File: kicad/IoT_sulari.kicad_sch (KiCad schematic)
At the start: 2 parts, among them U1 NRF9160-SICA-B1A-R, U2 TCR2EF33

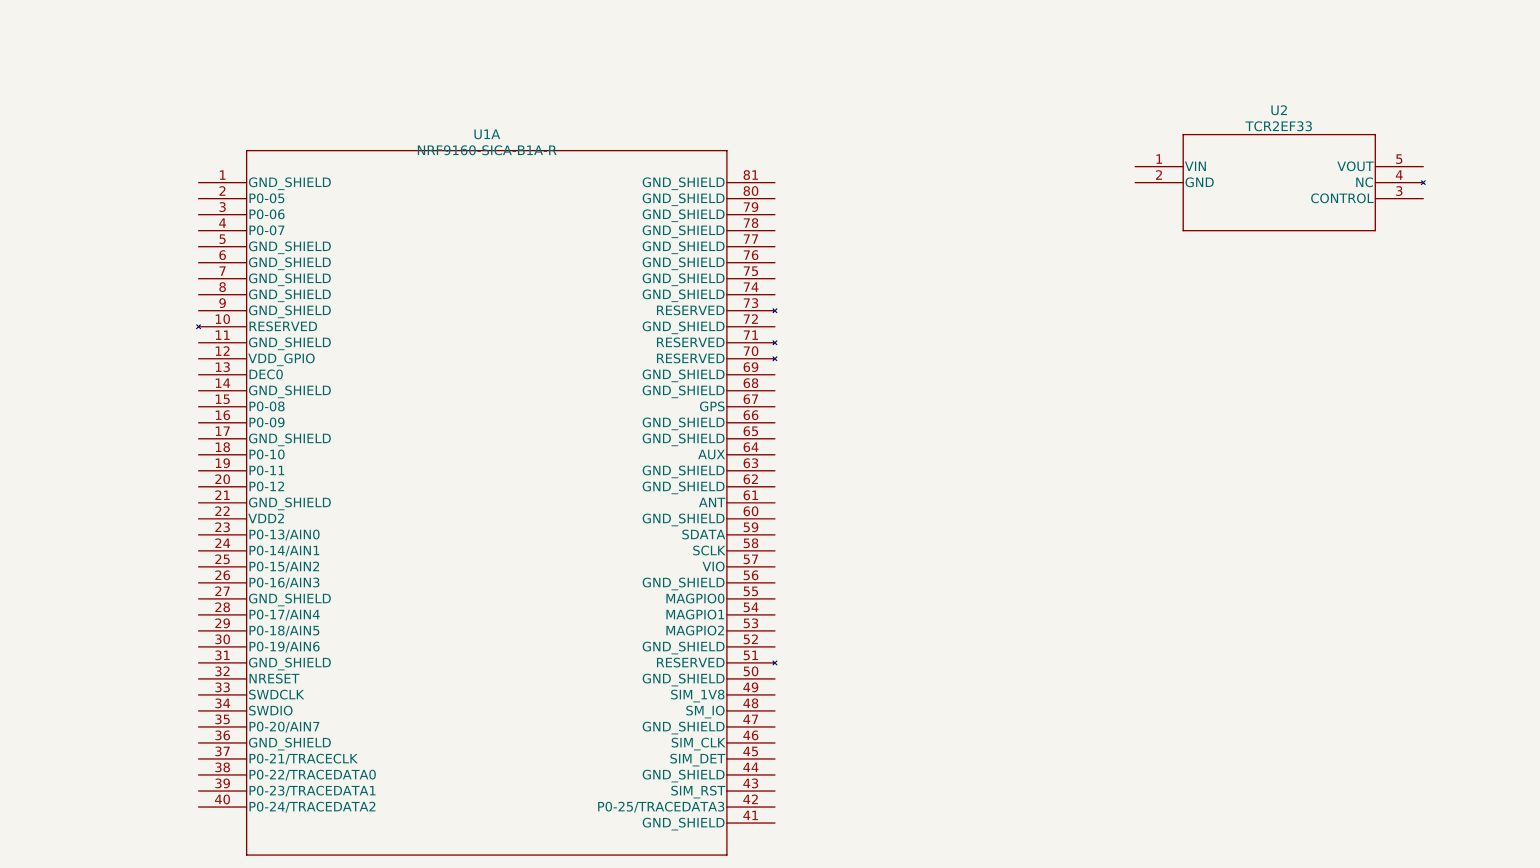
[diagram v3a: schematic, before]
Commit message: Added TMP117, HDC2010, TPD3F3 and TCR2EF33 symbols to KiCad and component documents to doc.
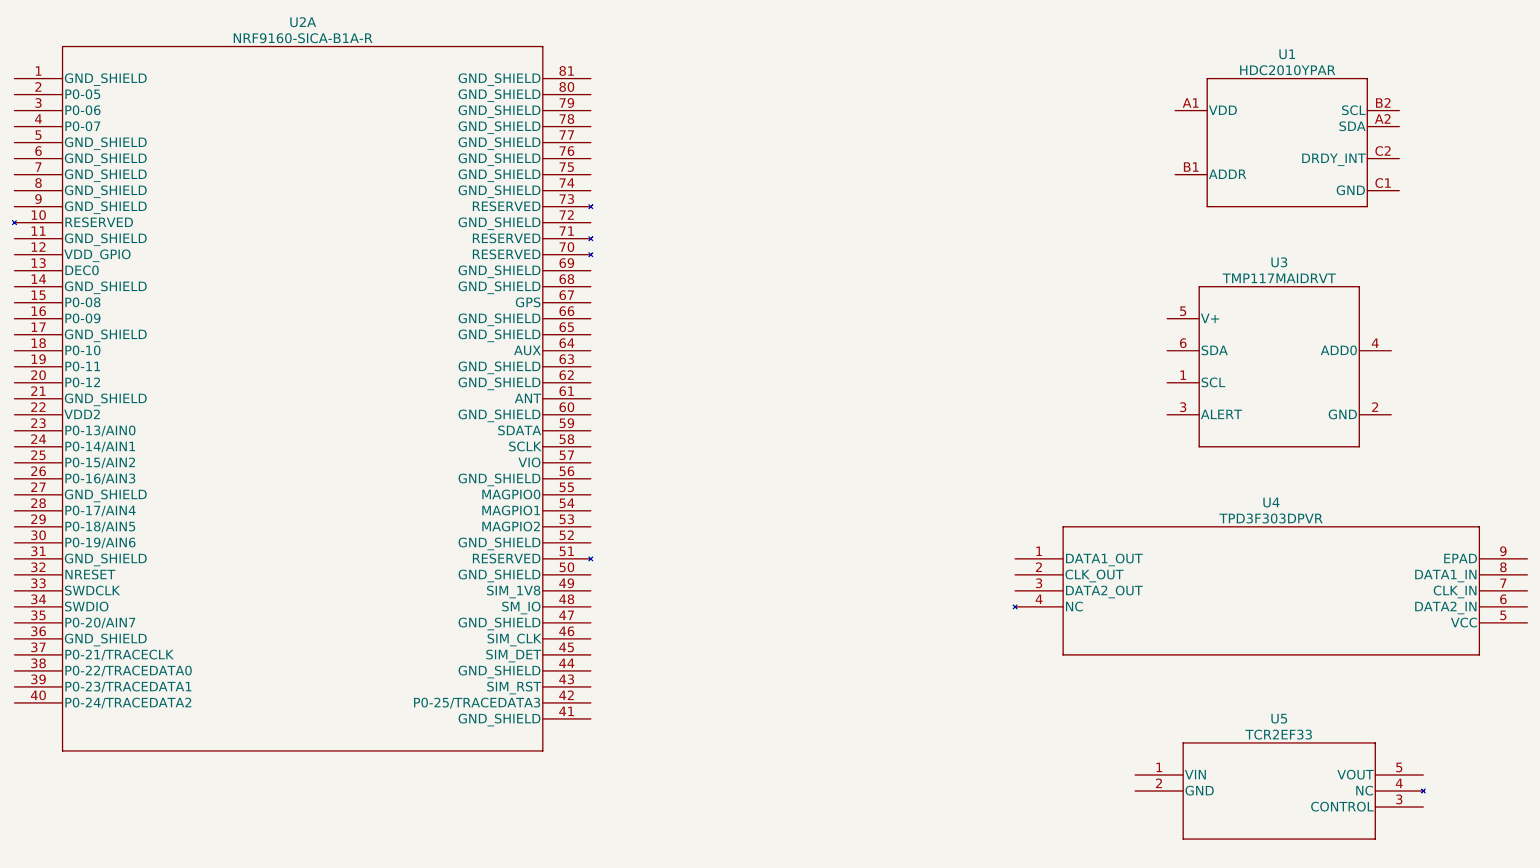
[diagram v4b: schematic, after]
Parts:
- removed U1: NRF9160-SICA-B1A-R, LGA_16X10P5_NOR, symbol NRF-9160-SICA-B1A-R:NRF9160-SICA-B1A-R
- removed U2: TCR2EF33, SOT-25 SMV_TOS, symbol TCR2EF33:TCR2EF33
- added U1: HDC2010YPAR, HDC2010YPAR:HDC2020YPAR, symbol HDC2010YPAR:HDC2010YPAR
- added U2: NRF9160-SICA-B1A-R, NRF-9160-SICA-B1A-R:NRF9160-SICA-B1A-R, symbol NRF-9160-SICA-B1A-R:NRF9160-SICA-B1A-R
- added U3: TMP117MAIDRVT, TMP117MAIDRVT:TMP117MAIDRVT, symbol TMP117MAIDRVT:TMP117MAIDRVT
- added U4: TPD3F303DPVR, TPD3F303DPVR:TPD3F303DPVR, symbol TPD3F303DPVR:TPD3F303DPVR
- added U5: TCR2EF33, TCR2EF33:TCR2EF33, symbol TCR2EF33:TCR2EF33
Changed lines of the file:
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@@
 (kicad_sch (version 20230121) (generator eeschema)
   (paper "A4")
-  (symbol (lib_id "TCR2EF33:TCR2EF33") (at 210.82 40.64 0) (unit 1)
-    (in_bom yes) (on_board yes) (dnp no) (fields_autoplaced)
-    (property "Reference" "U2" (at 233.68 31.75 0)
-      (effects (font (size 1.524 1.524)))
-    )
-    (property "Value" "TCR2EF33" (at 233.68 34.29 0)
-      (effects (font (size 1.524 1.524)))
-    )
-    (property "Footprint" "SOT-25   SMV_TOS" (at 233.68 34.544 0)
-      (effects (font (size 1.524 1.524)) hide)
-    )
-    (property "Datasheet" "" (at 210.82 40.64 0)
-      (effects (font (size 1.524 1.524)))
-    )
-    (pin "1")
-    (pin "2")
-    (pin "3")
-    (pin "4")
-    (pin "5")
-    (instances
-      (project "IoT_sulari"
-        (path "/184b47ed-2c2b-4c02-be35-d18f4f4e5685"
-          (reference "U2") (unit 1)
-        )
-      )
-    )
-  )
-  (symbol (lib_id "NRF-9160-SICA-B1A-R:NRF9160-SICA-B1A-R") (at 62.23 43.18 0) (unit 1)
-    (in_bom yes) (on_board yes) (dnp no) (fields_autoplaced)
-    (property "Reference" "U1" (at 107.95 35.56 0)
-      (effects (font (size 1.524 1.524)))
-    )
-    (property "Value" "NRF9160-SICA-B1A-R" (at 107.95 38.1 0)
-      (effects (font (size 1.524 1.524)))
-    )
-    (property "Footprint" "LGA_16X10P5_NOR" (at 107.95 37.084 0)
-      (effects (font (size 1.524 1.524)) hide)
-    )
-    (property "Datasheet" "" (at 62.23 43.18 0)
+  (symbol (lib_id "NRF-9160-SICA-B1A-R:NRF9160-SICA-B1A-R") (at 33.02 26.67 0) (unit 1)
+    (in_bom yes) (on_board yes) (dnp no) (fields_autoplaced)
+    (property "Reference" "U2" (at 78.74 17.78 0)
+      (effects (font (size 1.524 1.524)))
+    )
+    (property "Value" "NRF9160-SICA-B1A-R" (at 78.74 20.32 0)
+      (effects (font (size 1.524 1.524)))
+    )
+    (property "Footprint" "NRF-9160-SICA-B1A-R:NRF9160-SICA-B1A-R" (at 78.74 20.574 0)
+      (effects (font (size 1.524 1.524)) hide)
+    )
+    (property "Datasheet" "" (at 33.02 26.67 0)
       (effects (font (size 1.524 1.524)))
     )
@@
     (instances
       (project "IoT_sulari"
+        (path "/184b47ed-2c2b-4c02-be35-d18f4f4e5685"
+          (reference "U2") (unit 1)
+        )
+      )
+    )
+  )
+  (symbol (lib_id "TCR2EF33:TCR2EF33") (at 210.82 137.16 0) (unit 1)
+    (in_bom yes) (on_board yes) (dnp no) (fields_autoplaced)
+    (property "Reference" "U5" (at 233.68 128.27 0)
+      (effects (font (size 1.524 1.524)))
+    )
+    (property "Value" "TCR2EF33" (at 233.68 130.81 0)
+      (effects (font (size 1.524 1.524)))
+    )
+    (property "Footprint" "TCR2EF33:TCR2EF33" (at 233.68 131.064 0)
+      (effects (font (size 1.524 1.524)) hide)
+    )
+    (property "Datasheet" "" (at 210.82 137.16 0)
+      (effects (font (size 1.524 1.524)))
+    )
+    (pin "1")
+    (pin "2")
+    (pin "3")
+    (pin "4")
+    (pin "5")
+    (instances
+      (project "IoT_sulari"
+        (path "/184b47ed-2c2b-4c02-be35-d18f4f4e5685"
+          (reference "U5") (unit 1)
+        )
+      )
+    )
+  )
+  (symbol (lib_id "TMP117MAIDRVT:TMP117MAIDRVT") (at 233.68 72.39 0) (unit 1)
+    (in_bom yes) (on_board yes) (dnp no) (fields_autoplaced)
+    (property "Reference" "U3" (at 233.68 55.88 0)
+      (effects (font (size 1.524 1.524)))
+    )
+    (property "Value" "TMP117MAIDRVT" (at 233.68 58.42 0)
+      (effects (font (size 1.524 1.524)))
+    )
+    (property "Footprint" "TMP117MAIDRVT:TMP117MAIDRVT" (at 233.68 73.914 0)
+      (effects (font (size 1.524 1.524)) hide)
+    )
+    (property "Datasheet" "" (at 233.68 72.39 0)
+      (effects (font (size 1.524 1.524)))
+    )
+    (pin "1")
+    (pin "2")
+    (pin "3")
+    (pin "4")
+    (pin "5")
+    (pin "6")
+    (instances
+      (project "IoT_sulari"
+        (path "/184b47ed-2c2b-4c02-be35-d18f4f4e5685"
+          (reference "U3") (unit 1)
+        )
+      )
+    )
+  )
+  (symbol (lib_id "TPD3F303DPVR:TPD3F303DPVR") (at 191.77 102.87 0) (unit 1)
+    (in_bom yes) (on_board yes) (dnp no) (fields_autoplaced)
+    (property "Reference" "U4" (at 232.41 93.98 0)
+      (effects (font (size 1.524 1.524)))
+    )
+    (property "Value" "TPD3F303DPVR" (at 232.41 96.52 0)
+      (effects (font (size 1.524 1.524)))
+    )
+    (property "Footprint" "TPD3F303DPVR:TPD3F303DPVR" (at 232.41 96.774 0)
+      (effects (font (size 1.524 1.524)) hide)
+    )
+    (property "Datasheet" "" (at 191.77 102.87 0)
+      (effects (font (size 1.524 1.524)))
+    )
+    (pin "1")
+    (pin "2")
+    (pin "3")
+    (pin "4")
+    (pin "5")
+    (pin "6")
+    (pin "7")
+    (pin "8")
+    (pin "9")
+    (instances
+      (project "IoT_sulari"
+        (path "/184b47ed-2c2b-4c02-be35-d18f4f4e5685"
+          (reference "U4") (unit 1)
+        )
+      )
+    )
+  )
+  (symbol (lib_id "HDC2010YPAR:HDC2010YPAR") (at 234.95 36.83 0) (unit 1)
+    (in_bom yes) (on_board yes) (dnp no) (fields_autoplaced)
+    (property "Reference" "U1" (at 234.95 22.86 0)
+      (effects (font (size 1.524 1.524)))
+    )
+    (property "Value" "HDC2010YPAR" (at 234.95 25.4 0)
+      (effects (font (size 1.524 1.524)))
+    )
+    (property "Footprint" "HDC2010YPAR:HDC2020YPAR" (at 234.95 38.354 0)
+      (effects (font (size 1.524 1.524)) hide)
+    )
+    (property "Datasheet" "" (at 234.95 36.83 0)
+      (effects (font (size 1.524 1.524)))
+    )
+    (pin "A1")
+    (pin "A2")
+    (pin "B1")
+    (pin "B2")
+    (pin "C1")
+    (pin "C2")
+    (instances
+      (project "IoT_sulari"

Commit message: Added hierarchical sheets to different components
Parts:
- removed U1: HDC2010YPAR, HDC2010YPAR:HDC2020YPAR, symbol HDC2010YPAR:HDC2010YPAR
- removed U3: TMP117MAIDRVT, TMP117MAIDRVT:TMP117MAIDRVT, symbol TMP117MAIDRVT:TMP117MAIDRVT
- removed U4: TPD3F303DPVR, TPD3F303DPVR:TPD3F303DPVR, symbol TPD3F303DPVR:TPD3F303DPVR
- removed U5: TCR2EF33, TCR2EF33:TCR2EF33, symbol TCR2EF33:TCR2EF33
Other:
- added sheet sensorboard (sensorboard.kicad_sch)
- added sheet sim_module (sim_module.kicad_sch)
- added sheet voltage_regulator (voltage_regulator.kicad_sch)
- moved on the sheet: U2A
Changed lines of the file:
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@@
 (kicad_sch (version 20230121) (generator eeschema)
   (paper "A4")
-  (symbol (lib_id "NRF-9160-SICA-B1A-R:NRF9160-SICA-B1A-R") (at 33.02 26.67 0) (unit 1)
+  (symbol (lib_id "NRF-9160-SICA-B1A-R:NRF9160-SICA-B1A-R") (at 88.9 40.64 0) (unit 1)
     (in_bom yes) (on_board yes) (dnp no) (fields_autoplaced)
-    (property "Reference" "U2" (at 78.74 17.78 0)
+    (property "Reference" "U2" (at 134.62 31.75 0)
       (effects (font (size 1.524 1.524)))
     )
-    (property "Value" "NRF9160-SICA-B1A-R" (at 78.74 20.32 0)
+    (property "Value" "NRF9160-SICA-B1A-R" (at 134.62 34.29 0)
       (effects (font (size 1.524 1.524)))
     )
-    (property "Footprint" "NRF-9160-SICA-B1A-R:NRF9160-SICA-B1A-R" (at 78.74 20.574 0)
+    (property "Footprint" "NRF-9160-SICA-B1A-R:NRF9160-SICA-B1A-R" (at 134.62 34.544 0)
       (effects (font (size 1.524 1.524)) hide)
     )
-    (property "Datasheet" "" (at 33.02 26.67 0)
+    (property "Datasheet" "" (at 88.9 40.64 0)
       (effects (font (size 1.524 1.524)))
     )
@@
     )
   )
-  (symbol (lib_id "TCR2EF33:TCR2EF33") (at 210.82 137.16 0) (unit 1)
-    (in_bom yes) (on_board yes) (dnp no) (fields_autoplaced)
-    (property "Reference" "U5" (at 233.68 128.27 0)
-      (effects (font (size 1.524 1.524)))
-    )
-    (property "Value" "TCR2EF33" (at 233.68 130.81 0)
-      (effects (font (size 1.524 1.524)))
-    )
-    (property "Footprint" "TCR2EF33:TCR2EF33" (at 233.68 131.064 0)
-      (effects (font (size 1.524 1.524)) hide)
-    )
-    (property "Datasheet" "" (at 210.82 137.16 0)
-      (effects (font (size 1.524 1.524)))
-    )
-    (pin "1")
-    (pin "2")
-    (pin "3")
-    (pin "4")
-    (pin "5")
-    (instances
-      (project "IoT_sulari"
-        (path "/184b47ed-2c2b-4c02-be35-d18f4f4e5685"
-          (reference "U5") (unit 1)
-        )
+  (sheet (at 317.5 114.3) (size 125.73 92.71) (fields_autoplaced)
+    (stroke (width 0.1524) (type solid))
+    (fill (color 0 0 0 0.0000))
+    (property "Sheetname" "sim_module" (at 317.5 113.5884 0)
+      (effects (font (size 1.27 1.27)) (justify left bottom))
+    )
+    (property "Sheetfile" "sim_module.kicad_sch" (at 317.5 207.5946 0)
+      (effects (font (size 1.27 1.27)) (justify left top))
+    )
+    (instances
+      (project "IoT_sulari"
+        (path "/184b47ed-2c2b-4c02-be35-d18f4f4e5685" (page "4"))
       )
     )
   )
-  (symbol (lib_id "TMP117MAIDRVT:TMP117MAIDRVT") (at 233.68 72.39 0) (unit 1)
-    (in_bom yes) (on_board yes) (dnp no) (fields_autoplaced)
-    (property "Reference" "U3" (at 233.68 55.88 0)
-      (effects (font (size 1.524 1.524)))
-    )
-    (property "Value" "TMP117MAIDRVT" (at 233.68 58.42 0)
-      (effects (font (size 1.524 1.524)))
-    )
-    (property "Footprint" "TMP117MAIDRVT:TMP117MAIDRVT" (at 233.68 73.914 0)
-      (effects (font (size 1.524 1.524)) hide)
-    )
-    (property "Datasheet" "" (at 233.68 72.39 0)
-      (effects (font (size 1.524 1.524)))
-    )
-    (pin "1")
-    (pin "2")
-    (pin "3")
-    (pin "4")
-    (pin "5")
-    (pin "6")
-    (instances
-      (project "IoT_sulari"
-        (path "/184b47ed-2c2b-4c02-be35-d18f4f4e5685"
-          (reference "U3") (unit 1)
-        )
+  (sheet (at -147.32 121.92) (size 138.43 87.63) (fields_autoplaced)
+    (stroke (width 0.1524) (type solid))
+    (fill (color 0 0 0 0.0000))
+    (property "Sheetname" "voltage_regulator" (at -147.32 121.2084 0)
+      (effects (font (size 1.27 1.27)) (justify left bottom))
+    )
+    (property "Sheetfile" "voltage_regulator.kicad_sch" (at -147.32 210.1346 0)
+      (effects (font (size 1.27 1.27)) (justify left top))
+    )
+    (instances
+      (project "IoT_sulari"
+        (path "/184b47ed-2c2b-4c02-be35-d18f4f4e5685" (page "2"))
       )
     )
   )
-  (symbol (lib_id "TPD3F303DPVR:TPD3F303DPVR") (at 191.77 102.87 0) (unit 1)
-    (in_bom yes) (on_board yes) (dnp no) (fields_autoplaced)
-    (property "Reference" "U4" (at 232.41 93.98 0)
-      (effects (font (size 1.524 1.524)))
-    )
-    (property "Value" "TPD3F303DPVR" (at 232.41 96.52 0)
-      (effects (font (size 1.524 1.524)))
-    )
-    (property "Footprint" "TPD3F303DPVR:TPD3F303DPVR" (at 232.41 96.774 0)
-      (effects (font (size 1.524 1.524)) hide)
-    )
-    (property "Datasheet" "" (at 191.77 102.87 0)
-      (effects (font (size 1.524 1.524)))
-    )
-    (pin "1")
-    (pin "2")
-    (pin "3")
-    (pin "4")
-    (pin "5")
-    (pin "6")
-    (pin "7")
-    (pin "8")
-    (pin "9")
-    (instances
-      (project "IoT_sulari"
-        (path "/184b47ed-2c2b-4c02-be35-d18f4f4e5685"
-          (reference "U4") (unit 1)
-        )
-      )
-    )
-  )
-  (symbol (lib_id "HDC2010YPAR:HDC2010YPAR") (at 234.95 36.83 0) (unit 1)
-    (in_bom yes) (on_board yes) (dnp no) (fields_autoplaced)
-    (property "Reference" "U1" (at 234.95 22.86 0)
-      (effects (font (size 1.524 1.524)))
-    )
-    (property "Value" "HDC2010YPAR" (at 234.95 25.4 0)
-      (effects (font (size 1.524 1.524)))
-    )
-    (property "Footprint" "HDC2010YPAR:HDC2020YPAR" (at 234.95 38.354 0)
-      (effects (font (size 1.524 1.524)) hide)
-    )
-    (property "Datasheet" "" (at 234.95 36.83 0)
-      (effects (font (size 1.524 1.524)))
-    )
-    (pin "A1")
-    (pin "A2")
-    (pin "B1")
-    (pin "B2")
-    (pin "C1")
-    (pin "C2")
-    (instances
-      (project "IoT_sulari"
-        (path "/184b47ed-2c2b-4c02-be35-d18f4f4e5685"
-          (reference "U1") (unit 1)
-        )
-      )
-    )
+  (sheet (at 317.5 5.08) (size 125.73 90.17) (fields_autoplaced)
+    (stroke (width 0.1524) (type solid))
+    (fill (color 0 0 0 0.0000))
+    (property "Sheetname" "sensorboard" (at 317.5 4.3684 0)
+      (effects (font (size 1.27 1.27)) (justify left bottom))
+    )
+    (property "Sheetfile" "sensorboard.kicad_sch" (at 317.5 95.8346 0)
+      (effects (font (size 1.27 1.27)) (justify left top))
+    )
+    (instances
+      (project "IoT_sulari"
+        (path "/184b47ed-2c2b-4c02-be35-d18f4f4e5685" (page "3"))
+      )
+    )
